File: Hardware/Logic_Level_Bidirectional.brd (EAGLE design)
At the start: 15.2 x 12.7 mm, 19 parts, among them Q1 BSS138, Q2 BSS138, Q3 BSS138, Q4 BSS138

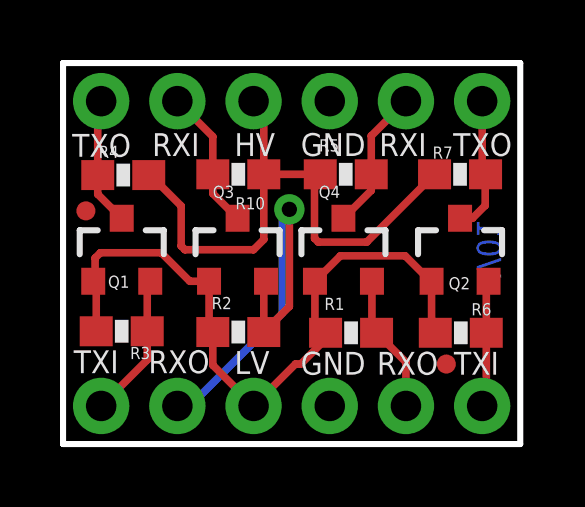
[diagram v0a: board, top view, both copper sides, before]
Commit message: Updated Schematic Frame
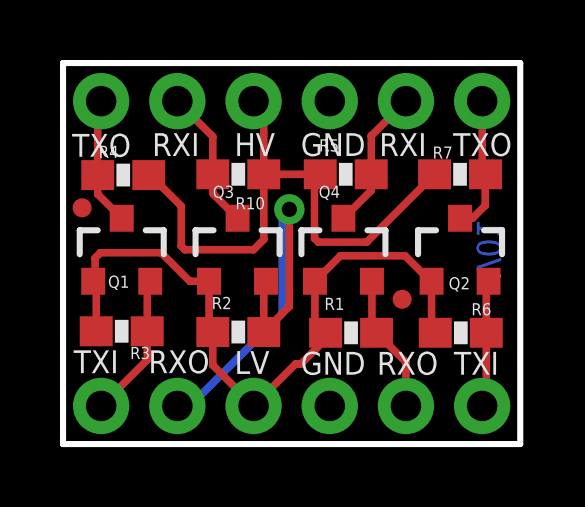
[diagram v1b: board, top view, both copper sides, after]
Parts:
- removed CC_TEXT1: CREATIVE_COMMONS, SparkFun-Aesthetics:CREATIVE_COMMONS
- JP3, JP4: device SparkFun:MICRO-FIDUCIAL -> SparkFun-Aesthetics:MICRO-FIDUCIAL
- moved JP3 13.2 mm to (0.64, 7.87)
- moved JP4 10.9 mm to (11.3, 4.83)
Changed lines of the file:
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@@
 <text x="2.286" y="9.144" size="0.762" layer="22" font="vector" ratio="15" rot="MR0">TXO</text>
 <text x="4.699" y="9.144" size="0.762" layer="22" font="vector" ratio="15" rot="MR0">RXI</text>
-<text x="9.525" y="9.144" size="0.762" layer="22" font="vector" ratio="15" rot="MR0">HV</text>
-<text x="7.239" y="9.144" size="0.762" layer="22" font="vector" ratio="15" rot="MR0">GND</text>
+<text x="6.985" y="9.144" size="0.762" layer="22" font="vector" ratio="15" rot="MR0">HV</text>
+<text x="9.779" y="9.144" size="0.762" layer="22" font="vector" ratio="15" rot="MR0">GND</text>
 <text x="12.319" y="9.144" size="0.762" layer="22" font="vector" ratio="15" rot="MR0">RXI</text>
 <text x="14.986" y="9.144" size="0.762" layer="22" font="vector" ratio="15" rot="MR0">TXO</text>
@@
 <text x="12.319" y="2.794" size="0.762" layer="22" font="vector" ratio="15" rot="MR0">RXO</text>
 <text x="4.699" y="2.794" size="0.762" layer="22" font="vector" ratio="15" rot="MR0">RXO</text>
-<text x="9.398" y="2.794" size="0.762" layer="22" font="vector" ratio="15" rot="MR0">LV</text>
-<text x="7.239" y="2.794" size="0.762" layer="22" font="vector" ratio="15" rot="MR0">GND</text>
+<text x="6.858" y="2.794" size="0.762" layer="22" font="vector" ratio="15" rot="MR0">LV</text>
+<text x="9.779" y="2.794" size="0.762" layer="22" font="vector" ratio="15" rot="MR0">GND</text>
 <text x="0.3048" y="9.5758" size="0.762" layer="21" font="vector" ratio="15">TXO</text>
 <text x="13.0048" y="9.6012" size="0.762" layer="21" font="vector" ratio="15">TXO</text>
@@
 <element name="JP1" library="SparkFun" package="1X06" value="" x="13.97" y="1.27" rot="MR0"/>
 <element name="JP2" library="SparkFun" package="1X06" value="" x="1.27" y="11.43" rot="MR180"/>
-<element name="JP3" library="SparkFun" package="MICRO-FIDUCIAL" value="FIDUCIALUFIDUCIAL" x="12.7762" y="2.667"/>
-<element name="JP4" library="SparkFun" package="MICRO-FIDUCIAL" value="FIDUCIALUFIDUCIAL" x="0.762" y="7.7724"/>
-<element name="CC_TEXT1" library="SparkFun-Aesthetics" package="CREATIVE_COMMONS" value="CREATIVE_COMMONS" x="21.59" y="-7.62"/>
 <element name="Q3" library="SparkFun" package="SOT23-3" value="BSS138" x="5.8166" y="6.4262"/>
 <element name="R2" library="SparkFun" package="0603-RES" value="10K" x="5.842" y="3.7338"/>
@@
 <element name="U$3" library="SparkFun-Aesthetics" package="SFE-LOGO-FLAME" value="" x="9.9314" y="3.7592" rot="MR0"/>
 <element name="U$1" library="SparkFun-Aesthetics" package="OSHW-LOGO-S" value="" x="6.8072" y="5.1816" rot="MR270"/>
+<element name="JP3" library="SparkFun-Aesthetics" package="MICRO-FIDUCIAL" value="FIDUCIALUFIDUCIAL" x="0.635" y="7.874"/>
+<element name="JP4" library="SparkFun-Aesthetics" package="MICRO-FIDUCIAL" value="FIDUCIALUFIDUCIAL" x="11.303" y="4.826"/>
 </elements>
 <signals>

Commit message: Silk Change, Schematic Change
Added deviding lines for HV/LV passages and change silk names as well
from RXO/TXO to HV1 LV2...etc as well as cleaned up the schematic.
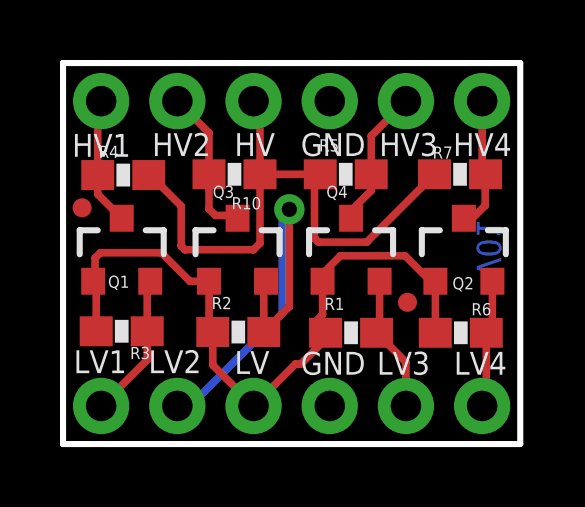
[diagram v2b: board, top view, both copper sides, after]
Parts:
- removed U$1: (no value), SparkFun-Aesthetics:OSHW-LOGO-S
- removed U$3: (no value), SparkFun-Aesthetics:SFE-LOGO-FLAME
- added LOGO1: SFE_LOGO_FLAME.1_INCH, SparkFun-Aesthetics:SFE_LOGO_FLAME_.1
- added LOGO2: OSHW-LOGOS, SparkFun-Aesthetics:OSHW-LOGO-S
- moved Q4 0.25 mm to (9.60, 6.43)
- moved JP4 0.20 mm to (11.5, 4.72)
- moved Q2 0.13 mm to (13.4, 6.43)
- moved R10 0.13 mm to (5.71, 8.99)
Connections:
- net RX2_HV renamed HV3
- net RX2_LV renamed LV3
- net RX_HV renamed HV2
- net RX_LV renamed LV2
- net TX2_HV renamed HV4
- net TX2_LV renamed LV4
- net TX_HV renamed HV1
- net TX_LV renamed LV1
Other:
- board text added: "HV1"
- board text added: "HV2"
- board text added: "HV3"
- board text added: "HV4"
- board text added: "LV1"
- board text added: "LV2"
- board text added: "LV3"
- board text added: "LV4"
- board text removed: "CHAN1"
- board text removed: "CHAN2"
- board text removed: "RXI"
- board text removed: "RXO"
- board text removed: "TXI"
- board text removed: "TXO"
